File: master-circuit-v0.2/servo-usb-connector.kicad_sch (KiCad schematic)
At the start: 12 parts

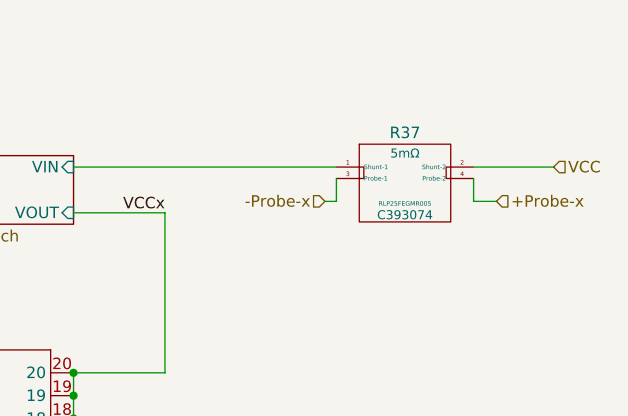
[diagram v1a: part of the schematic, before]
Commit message: Drop unused features and arrange components on new master circuit board.
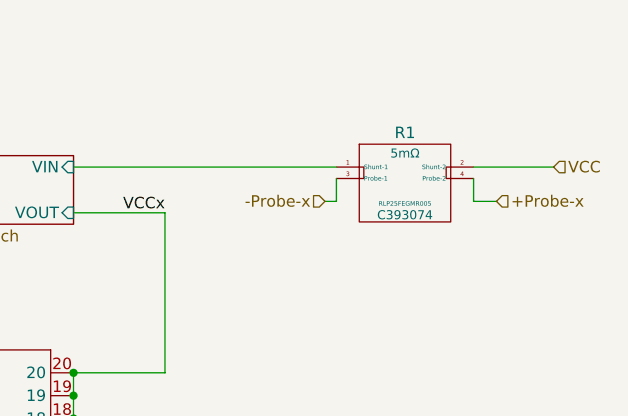
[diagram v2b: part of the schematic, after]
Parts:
- renumbered R37 to R1
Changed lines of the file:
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@@
 		(instances
 			(project "master-circuit"
-				(path "/240d81ac-e9d7-42ea-a748-33df14683b07/0e9db04d-03bc-47ea-840c-10fa3db91e46"
-					(reference "FPC7")
-					(unit 1)
-				)
 				(path "/240d81ac-e9d7-42ea-a748-33df14683b07/3be7b3c1-0262-49c7-a4f6-ac91c068130a"
 					(reference "FPC1")
@@
 		(instances
 			(project "master-circuit"
-				(path "/240d81ac-e9d7-42ea-a748-33df14683b07/0e9db04d-03bc-47ea-840c-10fa3db91e46"
-					(reference "#PWR080")
-					(unit 1)
-				)
 				(path "/240d81ac-e9d7-42ea-a748-33df14683b07/3be7b3c1-0262-49c7-a4f6-ac91c068130a"
 					(reference "#PWR07")
@@
 		(instances
 			(project "master-circuit"
-				(path "/240d81ac-e9d7-42ea-a748-33df14683b07/0e9db04d-03bc-47ea-840c-10fa3db91e46"
-					(reference "R109")
-					(unit 1)
-				)
 				(path "/240d81ac-e9d7-42ea-a748-33df14683b07/3be7b3c1-0262-49c7-a4f6-ac91c068130a"
 					(reference "R103")
@@
 		(instances
 			(project "master-circuit"
-				(path "/240d81ac-e9d7-42ea-a748-33df14683b07/0e9db04d-03bc-47ea-840c-10fa3db91e46"
-					(reference "R72")
-					(unit 1)
-				)
 				(path "/240d81ac-e9d7-42ea-a748-33df14683b07/3be7b3c1-0262-49c7-a4f6-ac91c068130a"
 					(reference "R35")
@@
 		(instances
 			(project "master-circuit"
-				(path "/240d81ac-e9d7-42ea-a748-33df14683b07/0e9db04d-03bc-47ea-840c-10fa3db91e46"
-					(reference "#PWR083")
-					(unit 1)
-				)
 				(path "/240d81ac-e9d7-42ea-a748-33df14683b07/3be7b3c1-0262-49c7-a4f6-ac91c068130a"
 					(reference "#PWR09")
@@
 		(instances
 			(project "master-circuit"
-				(path "/240d81ac-e9d7-42ea-a748-33df14683b07/0e9db04d-03bc-47ea-840c-10fa3db91e46"
-					(reference "C41")
-					(unit 1)
-				)
 				(path "/240d81ac-e9d7-42ea-a748-33df14683b07/3be7b3c1-0262-49c7-a4f6-ac91c068130a"
 					(reference "C15")
@@
 		(instances
 			(project "master-circuit"
-				(path "/240d81ac-e9d7-42ea-a748-33df14683b07/0e9db04d-03bc-47ea-840c-10fa3db91e46"
-					(reference "#PWR081")
-					(unit 1)
-				)
 				(path "/240d81ac-e9d7-42ea-a748-33df14683b07/3be7b3c1-0262-49c7-a4f6-ac91c068130a"
 					(reference "#PWR053")
@@
 		(instances
 			(project "master-circuit"
-				(path "/240d81ac-e9d7-42ea-a748-33df14683b07/0e9db04d-03bc-47ea-840c-10fa3db91e46"
-					(reference "U34")
-					(unit 1)
-				)
 				(path "/240d81ac-e9d7-42ea-a748-33df14683b07/3be7b3c1-0262-49c7-a4f6-ac91c068130a"
 					(reference "U7")
@@
 		(instances
 			(project "master-circuit"
-				(path "/240d81ac-e9d7-42ea-a748-33df14683b07/0e9db04d-03bc-47ea-840c-10fa3db91e46"
-					(reference "R90")
-					(unit 1)
-				)
 				(path "/240d81ac-e9d7-42ea-a748-33df14683b07/3be7b3c1-0262-49c7-a4f6-ac91c068130a"
 					(reference "R76")
@@
 		(instances
 			(project "master-circuit"
-				(path "/240d81ac-e9d7-42ea-a748-33df14683b07/0e9db04d-03bc-47ea-840c-10fa3db91e46"
-					(reference "R77")
-					(unit 1)
-				)
 				(path "/240d81ac-e9d7-42ea-a748-33df14683b07/3be7b3c1-0262-49c7-a4f6-ac91c068130a"
 					(reference "R13")
@@
 		(instances
 			(project "master-circuit"
-				(path "/240d81ac-e9d7-42ea-a748-33df14683b07/0e9db04d-03bc-47ea-840c-10fa3db91e46"
-					(reference "USB2")
-					(unit 1)
-				)
 				(path "/240d81ac-e9d7-42ea-a748-33df14683b07/3be7b3c1-0262-49c7-a4f6-ac91c068130a"
 					(reference "USB1")
@@
 				)
 				(path "/240d81ac-e9d7-42ea-a748-33df14683b07/45541b12-3178-4a35-ba98-195b0b7ec5c7"
+					(reference "USB4")
+					(unit 1)
+				)
+				(path "/240d81ac-e9d7-42ea-a748-33df14683b07/855ba32d-cbe2-4fa8-81ea-b92e9f1eee99"
 					(reference "USB5")
 					(unit 1)
 				)
-				(path "/240d81ac-e9d7-42ea-a748-33df14683b07/855ba32d-cbe2-4fa8-81ea-b92e9f1eee99"
+				(path "/240d81ac-e9d7-42ea-a748-33df14683b07/9cbab574-5c5a-48fe-8b65-ca60995f0183"
+					(reference "USB2")
+					(unit 1)
+				)
+				(path "/240d81ac-e9d7-42ea-a748-33df14683b07/c713c99b-333c-4e3a-a177-aa20b97ab5d6"
+					(reference "USB3")
+					(unit 1)
+				)
+				(path "/240d81ac-e9d7-42ea-a748-33df14683b07/e9d0615a-b417-460d-a006-9061a6883b3e"
 					(reference "USB6")
-					(unit 1)
-				)
-				(path "/240d81ac-e9d7-42ea-a748-33df14683b07/9cbab574-5c5a-48fe-8b65-ca60995f0183"
-					(reference "USB3")
-					(unit 1)
-				)
-				(path "/240d81ac-e9d7-42ea-a748-33df14683b07/c713c99b-333c-4e3a-a177-aa20b97ab5d6"
-					(reference "USB4")
-					(unit 1)
-				)
-				(path "/240d81ac-e9d7-42ea-a748-33df14683b07/e9d0615a-b417-460d-a006-9061a6883b3e"
-					(reference "USB7")
 					(unit 1)
 				)
@@
 		(instances
 			(project "master-circuit"
-				(path "/240d81ac-e9d7-42ea-a748-33df14683b07/0e9db04d-03bc-47ea-840c-10fa3db91e46"
-					(reference "R102")
-					(unit 1)
-				)
 				(path "/240d81ac-e9d7-42ea-a748-33df14683b07/3be7b3c1-0262-49c7-a4f6-ac91c068130a"
 					(reference "R96")
@@
 		(instances
 			(project "master-circuit"
-				(path "/240d81ac-e9d7-42ea-a748-33df14683b07/0e9db04d-03bc-47ea-840c-10fa3db91e46"
-					(reference "D12")
-					(unit 1)
-				)
 				(path "/240d81ac-e9d7-42ea-a748-33df14683b07/3be7b3c1-0262-49c7-a4f6-ac91c068130a"
 					(reference "D1")
@@
 		(instances
 			(project "master-circuit"
-				(path "/240d81ac-e9d7-42ea-a748-33df14683b07/0e9db04d-03bc-47ea-840c-10fa3db91e46"
-					(reference "#PWR082")
-					(unit 1)
-				)
 				(path "/240d81ac-e9d7-42ea-a748-33df14683b07/3be7b3c1-0262-49c7-a4f6-ac91c068130a"
 					(reference "#PWR08")
@@
 		(instances
 			(project "master-circuit"
-				(path "/240d81ac-e9d7-42ea-a748-33df14683b07/0e9db04d-03bc-47ea-840c-10fa3db91e46"
-					(reference "R92")
-					(unit 1)
-				)
 				(path "/240d81ac-e9d7-42ea-a748-33df14683b07/3be7b3c1-0262-49c7-a4f6-ac91c068130a"
 					(reference "R79")
@@
 		(dnp no)
 		(fields_autoplaced yes)
-		(property "Reference" "R37"
+		(property "Reference" "R1"
 			(at 252.73 38.1 0)
 			(show_name no)
@@
 		(instances
 			(project "master-circuit"
-				(path "/240d81ac-e9d7-42ea-a748-33df14683b07/0e9db04d-03bc-47ea-840c-10fa3db91e46"
-					(reference "R78")
-					(unit 1)
-				)
 				(path "/240d81ac-e9d7-42ea-a748-33df14683b07/3be7b3c1-0262-49c7-a4f6-ac91c068130a"
-					(reference "R37")
+					(reference "R1")
 					(unit 1)
 				)
 				(path "/240d81ac-e9d7-42ea-a748-33df14683b07/45541b12-3178-4a35-ba98-195b0b7ec5c7"
-					(reference "R68")
+					(reference "R4")
 					(unit 1)
 				)
 				(path "/240d81ac-e9d7-42ea-a748-33df14683b07/855ba32d-cbe2-4fa8-81ea-b92e9f1eee99"
-					(reference "R73")
+					(reference "R5")
 					(unit 1)
 				)
 				(path "/240d81ac-e9d7-42ea-a748-33df14683b07/9cbab574-5c5a-48fe-8b65-ca60995f0183"
-					(reference "R56")
+					(reference "R2")
 					(unit 1)
 				)
 				(path "/240d81ac-e9d7-42ea-a748-33df14683b07/c713c99b-333c-4e3a-a177-aa20b97ab5d6"
-					(reference "R62")
+					(reference "R3")
 					(unit 1)
 				)
 				(path "/240d81ac-e9d7-42ea-a748-33df14683b07/e9d0615a-b417-460d-a006-9061a6883b3e"
-					(reference "R74")
+					(reference "R6")
 					(unit 1)
 				)
@@
 		(instances
 			(project "master-circuit"
-				(path "/240d81ac-e9d7-42ea-a748-33df14683b07/0e9db04d-03bc-47ea-840c-10fa3db91e46"
-					(reference "#PWR084")
-					(unit 1)
-				)
 				(path "/240d81ac-e9d7-42ea-a748-33df14683b07/3be7b3c1-0262-49c7-a4f6-ac91c068130a"
 					(reference "#PWR041")
@@
 					(page "15")
 				)
-				(path "/240d81ac-e9d7-42ea-a748-33df14683b07/0e9db04d-03bc-47ea-840c-10fa3db91e46"
-					(page "17")
-				)
-			)
+			)

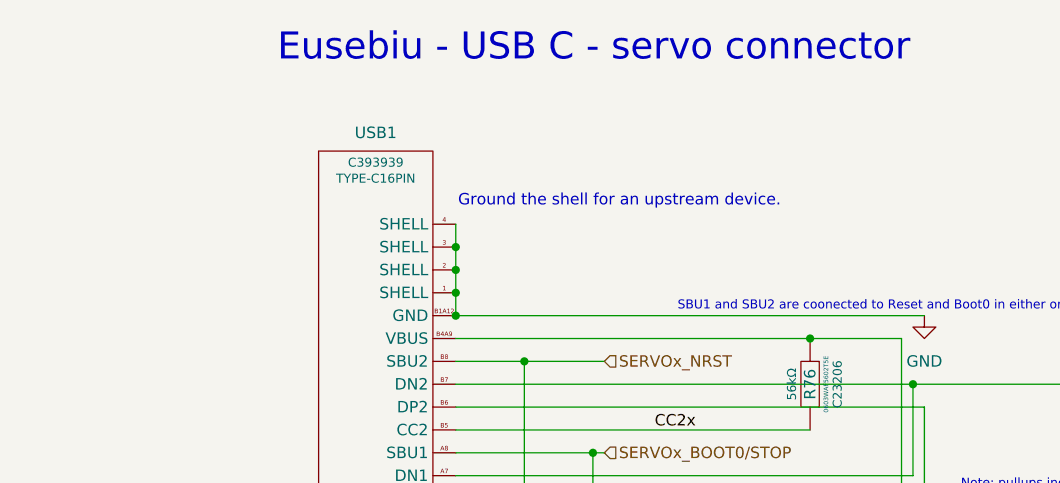
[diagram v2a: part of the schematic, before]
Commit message: Connect one of the USB outputs, outline part placement.
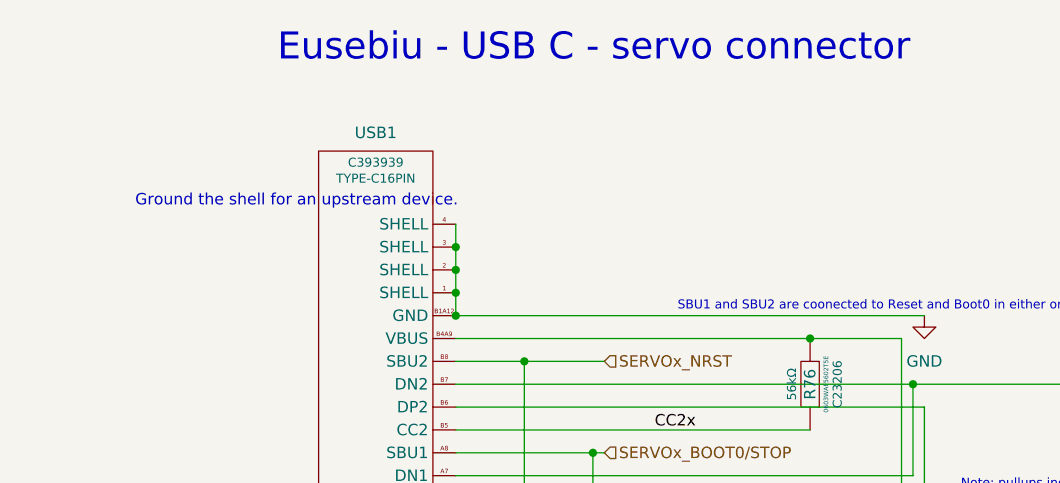
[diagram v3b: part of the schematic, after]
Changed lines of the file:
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@@
 				(size 1.27 1.27)
 			)
-			(justify left)
+			(justify right)
 		)
 	)

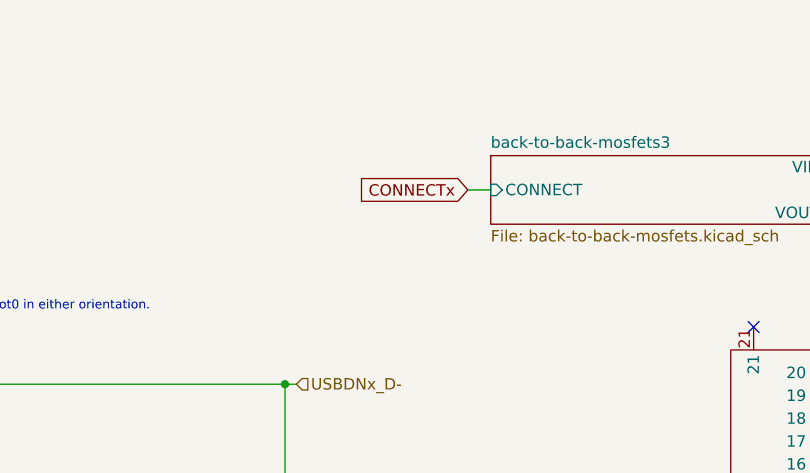
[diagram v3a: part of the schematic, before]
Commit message: USB hub lines remaining.
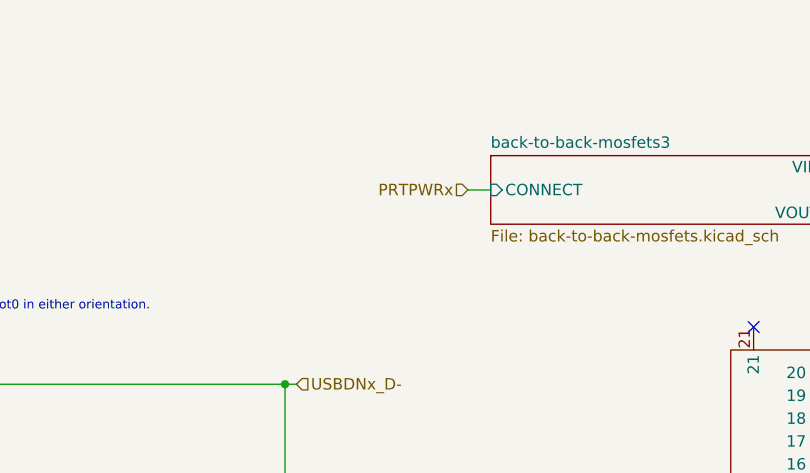
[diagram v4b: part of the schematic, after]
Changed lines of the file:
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@@
-		)
-	)
-	(global_label "CONNECTx"
-		(shape input)
-		(at 175.26 44.45 180)
-		(fields_autoplaced yes)
-		(effects
-			(font
-				(size 1.27 1.27)
-			)
-			(justify right)
-		)
-		(property "Intersheetrefs" "${INTERSHEET_REFS}"
-			(at 162.5986 44.45 0)
-			(hide yes)
-			(show_name no)
-			(do_not_autoplace no)
-			(effects
-				(font
-					(size 1.27 1.27)
-				)
-				(justify right)
-			)
 		)
 	)
@@
 		)
 	)
+	(hierarchical_label "PRTPWRx"
+		(shape input)
+		(at 175.26 44.45 180)
+		(effects
+			(font
+				(size 1.27 1.27)
+			)
+			(justify right)
+		)
+	)
